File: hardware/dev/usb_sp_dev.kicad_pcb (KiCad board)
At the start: 4 copper layers, 76.1 x 70.7 mm, 82 parts, among them P1 HDR-IDC-2_54-2X5P, P2 HDR-IDC-2_54-2X5P, U1 ZD24C02B-MAGMT, U10 RH-5015, U11 RH-5015, U12 RH-5015, U13 RH-5015, U14 RH-5015, U15 RH-5015, U16 RH-5015, U17 RH-5015, U18 KH-TYPE-C-16P, U19 CH32V203C8U6, U2 TC-6601-5_0-260-8_3, U20 TC-6601-5_0-260-8_3, U21 CH572D, U22 HX_PH254-01-04-Z-L11_5_STRAIG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, U23 KH-TYPE-C-16P, U24 RH-5015, U25 RH-5015, U26 DMG2305UX-7, U27 DMG2305UX-7, U28 DMG2305UX-7, U3 TC-6601-5_0-260-8_3, U33 HX_PH254-01-04-Z-L11_5_STRAIG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, U34 RH-5015, U35 RH-5015, U36 RH-5015, U37 RH-5015, U4 TC-6601-5_0-260-8_3, U5 SN74LVC1G32DBVR, U6 SN74LVC1G32DBVR, U7 SD101CWS, U8 PZ254V-11-03P_C2937625, U9 32.768kHz, X1 8MHz, X2 XTM20032000DT00351001

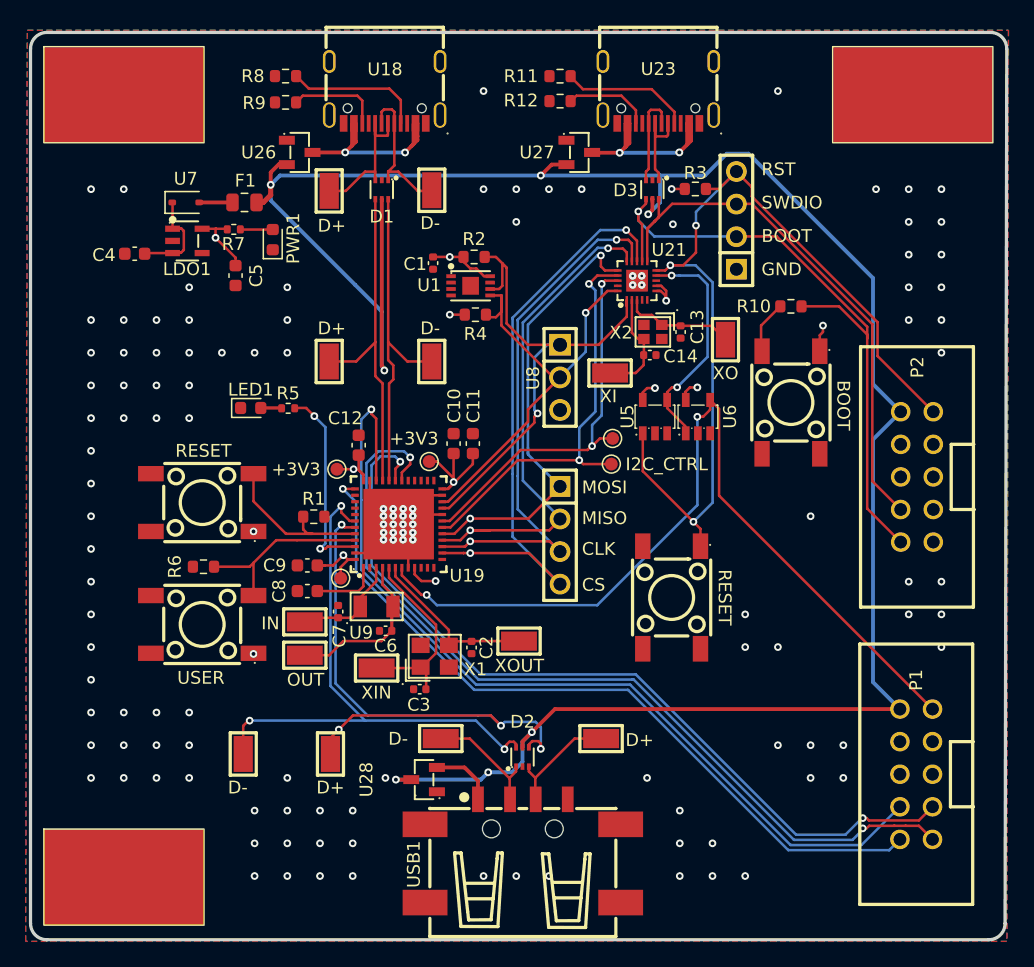
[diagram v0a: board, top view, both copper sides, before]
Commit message: feat(hardware-dev): replace mode transistors with TPS2121 power mux
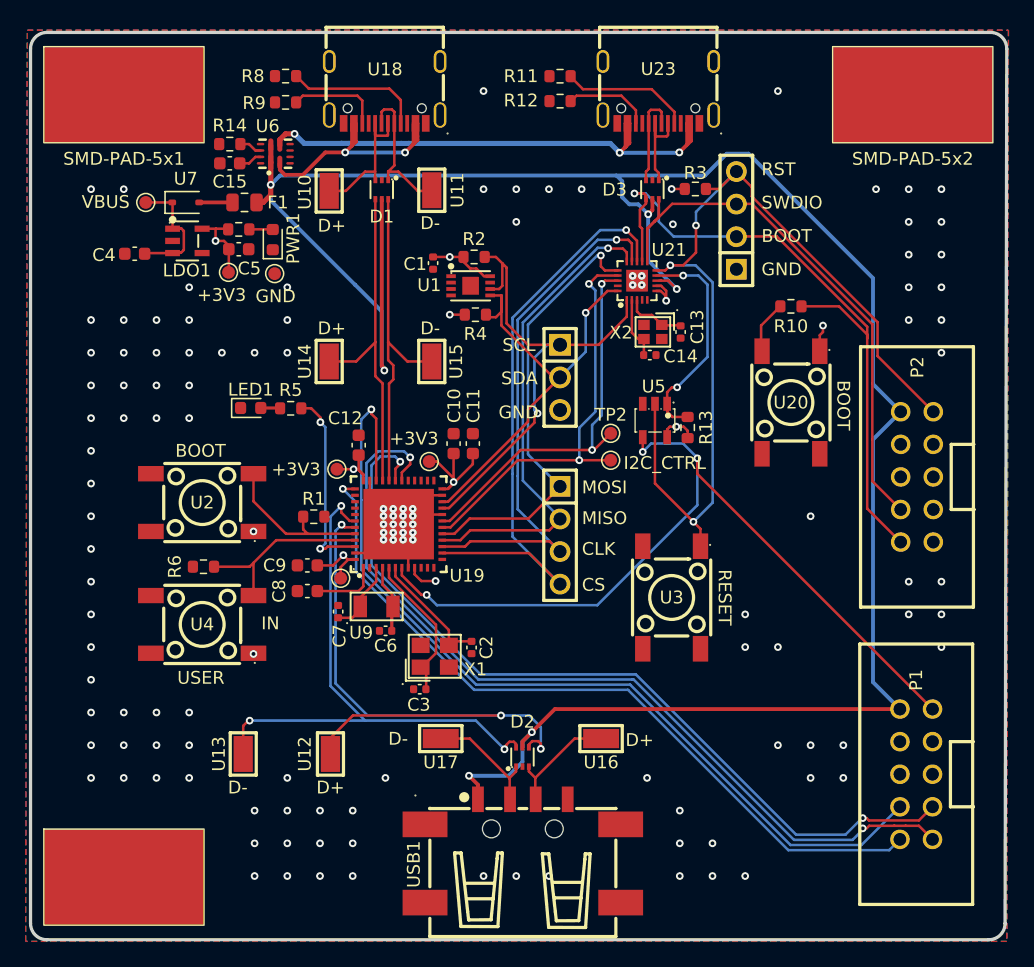
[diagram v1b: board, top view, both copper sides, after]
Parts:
- removed the U24 at (159.2, 93.5)
- removed U25, U34, U35, U36, U37: RH-5015, usb_sp_dev:SMD_RH-5015
- removed U26, U27, U28: DMG2305UX-7, usb_sp_dev:SOT-23-3_L2.9-W1.3-P1.90-LS2.4-BR
- added C15: 100nF, Capacitor_SMD:C_0603_1608Metric, F.Cu at (129.6, 77.1)
- added R13: 10kΩ, Resistor_SMD:R_0603_1608Metric, F.Cu at (165.3, 97.7)
- added R14: 25.5kΩ, Resistor_SMD:R_0603_1608Metric, F.Cu at (129.6, 75.6)
- added TP6: TestPoint, TestPoint:TestPoint_Pad_D1.0mm, F.Cu at (123.0, 80.2)
- added TP7: TestPoint, TestPoint:TestPoint_Pad_D1.0mm, F.Cu at (129.5, 85.6)
- added TP8: TestPoint, TestPoint:TestPoint_Pad_D1.0mm, F.Cu at (133.1, 85.7)
- R5, R7: footprint Resistor_SMD:R_0402_1005Metric -> Resistor_SMD:R_0603_1608Metric
- U5: value SN74LVC1G32DBVR -> SN74LVC1G08DBVR; footprint usb_sp:SOT-23-5_L3.0-W1.7-P0.95-LS2.8-BR -> usb_sp_dev:SOT-23-5_L3.0-W1.7-P0.95-LS2.8-BR
- U6: value SN74LVC1G32DBVR -> TPS2121RUXR; footprint usb_sp:SOT-23-5_L3.0-W1.7-P0.95-LS2.8-BR -> usb_sp:VQFN-HR-12_L2.5-W2.0-P0.50-BL
- moved U6 38.8 mm to (133.1, 76.4), turned to 0 degrees
- moved C5 2.07 mm to (130.3, 83.8), turned to 180 degrees
- moved TP2 0.43 mm to (159.3, 98.2)
- moved R7 0.39 mm to (130.3, 82.3)
- moved TP1 0.30 mm to (159.3, 100.3)
- moved U5 0.30 mm to (162.7, 97.2), turned to 90 degrees
- moved R5 0.20 mm to (134.3, 96.2)
- renumbered U33 to U24
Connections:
- U21 pad 8: +5V -> VBUS
- U5 pad 1: /CH32V203/RST -> /CH32V203/GPIO_RST_CH32
- U5 pad 2: GND -> /CH32V203/RST
- U5 pad 4: /CH32V203/GPIO_RST_CH32 -> /CH32V203/RST_CH32
- U6 pad 1: /CH32V203/GPIO_RST_CH32 -> VBUS
- U6 pad 2: GND -> USB_1_VBUS
- U6 pad 4: /CH32V203/RST_CH32 -> GND
- U6 pad 5: +3V3 -> GND
- USB1 pad 1: USB_OUT_VBUS -> VBUS
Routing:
- net USB_2_VBUS: track 16.3 -> 41.7 mm, vias 2 -> 3
- net /CH32V203/OSC32OUT: track 12.8 -> 5.19 mm
- net USB_OUT_VBUS: track 5.07 -> 0.00 mm
- net /CH32V203/XOUT: track 13.5 -> 9.23 mm
- net /CH32V203/XIN: track 15.2 -> 11.0 mm
- net /CH572D/XO: track 8.76 -> 4.77 mm
- net /CH32V203/OSC32IN: track 8.50 -> 4.82 mm
- net /CH572D/XI: track 8.62 -> 4.93 mm
- net USB_1_VBUS: track 16.3 -> 19.9 mm
- net /CH32V203/RST_CH32: track 67.9 -> 64.7 mm, vias 2 -> 3
- net VBUS: track 177.0 -> 179.6 mm, vias 7 -> 6
- net /CH572D/BOOT_0: track 51.4 -> 53.7 mm
- net GND: track 7.71 -> 5.43 mm
- net /CH32V203/VBUS_FUSED: track 7.50 -> 9.53 mm
- net Net-(U6-SS): track 0.00 -> 1.83 mm
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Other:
- board text added: "SCL"
- board text added: "SDA"
- board text added: "VBUS"
- board text removed: "OUT"
- board text removed: "XI"
- board text removed: "XIN"
- board text removed: "XO"
- board text removed: "XOUT"
